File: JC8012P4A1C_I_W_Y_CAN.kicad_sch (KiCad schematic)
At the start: 0 parts

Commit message: Add CAN transceiver and 12V->5V supply schematic
CAN interface (ISOBUS, 250 kbit/s):
- TLE9250VSJ transceiver, VCC 5 V, VIO 3.3 V from FPC3 VDDA
- TXD/RXD on FPC3 pin 8/7 (GPIO4/GPIO5, as used by espVT)
- NEN on FPC3 pin 9 (GPIO3) with 10k pull-down -> normal mode by default
- Split termination 750R + 750R, 47 nF to GND (ECU Type I WEAK)
- WE-TVS 824094024 on CAN_H/CAN_L
- 10-pin box header 61201022921 -> ribbon -> IDC D-Sub 9 female
  618009221923, pinout of Mueller-Elektronik BASIC-Terminal CAN-ISO
  (fits adapter cable 481595 to In-Cab CPC-9)

Power (12 V board net only):
- Fuse 1 A slow, bidirectional TVS WE-TVSP 824551241 (SMDJ24CA)
- Reverse polarity protection: dual P-MOSFET DMP6050SSD in parallel,
  15 V gate zener, 100k gate pull-down
- Wuerth MagI3C 171030601 buck, 5.0 V / 3 A, values from datasheet p.38
- 5 V fed to the transceiver and to the base board CN2 via WR-WTB
  653104131822

Pin 8 of the TLE9250VSJ symbol renamed STB -> NEN.

Co-Authored-By: Claude Opus 5.5 <noreply@anthropic.com>
Claude-Session: https://claude.ai/code/session_014h8cGi8SRWthYdGFH1Qgzz
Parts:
- added C1: 47n, Capacitor_SMD:C_0603_1608Metric, symbol Device:C
- added C2, C3: 100n, Capacitor_SMD:C_0603_1608Metric, symbol Device:C
- added C4: 10u/50V, Capacitor_SMD:C_1210_3225Metric, symbol Device:C
- added C5: 100u/10V, Capacitor_SMD:C_1210_3225Metric, symbol Device:C
- added C6, C7: 22n, Capacitor_SMD:C_0603_1608Metric, symbol Device:C
- added D1: 824094024, JC8012P4A1C_CAN:D_Wurth_WE-TVS-SOT23-3L, symbol JC8012P4A1C_CAN:824094024
- added D2: 824551241, JC8012P4A1C_CAN:D_Wurth_WE-TVSP-DO214-AB-3000W_BI, symbol Device:D_TVS
- added D3: 15V, Diode_SMD:D_SOD-123, symbol Device:D_Zener
- added F1: 1A slow, Fuse:Fuse_1206_3216Metric, symbol Device:Fuse
- added J1: 61201022921, JC8012P4A1C_CAN:J_Wurth_WR-BHD_61201022921, symbol JC8012P4A1C_CAN:61201022921
- added J2: 68711414522, JC8012P4A1C_CAN:J_Wurth_WR-FPC_68711414522, symbol JC8012P4A1C_CAN:68711414522
- added J3: 653104131822, JC8012P4A1C_CAN:J_Wurth_WR-WTB_653104131822, symbol JC8012P4A1C_CAN:653104131822
- added Q1: DMP6050SSD, Package_SO:SOIC-8_3.9x4.9mm_P1.27mm, symbol Transistor_FET:DMP6050SSD
- added R1, R2: 750, Resistor_SMD:R_0603_1608Metric, symbol Device:R
- added R3: 10k, Resistor_SMD:R_0603_1608Metric, symbol Device:R
- added R4, R5: 100k, Resistor_SMD:R_0603_1608Metric, symbol Device:R
- added R6: 5k62, Resistor_SMD:R_0603_1608Metric, symbol Device:R
- added R7: 1k07, Resistor_SMD:R_0603_1608Metric, symbol Device:R
- added U1: TLE9250VSJ, Package_SO:SOIC-8_3.9x4.9mm_P1.27mm, symbol JC8012P4A1C_CAN:TLE9250VSJ
- added U2: 171030601, JC8012P4A1C_CAN:U_Wurth_WPME-VDRM-TO263-7EP, symbol JC8012P4A1C_CAN:171030601
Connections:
- new net +3V3: C3.1, J2.13, J2.14, U1.5 (VIO)
- new net +5V: C2.1, C5.1, C7.1, J3.1, R6.1, U1.3 (VCC), U2.7 (VOUT)
- new net BUCK_FB: C7.2, R6.2, R7.1, U2.6 (FB)
- new net BUCK_RON: R5.2, U2.2 (RON)
- new net BUCK_SS: C6.1, U2.5 (SS)
- new net CAN_H: D1.1 (I/O1), J1.4, J1.7, R1.1, U1.7 (CANH)
- new net CAN_L: D1.2 (I/O2), J1.1, J1.3, R2.2, U1.6 (CANL)
- new net CAN_NEN: J2.9, R3.1, U1.8 (NEN)
- new net CAN_RXD: J2.7, U1.4 (RXD)
- new net CAN_SPLIT: C1.1, R1.2, R2.1
- new net CAN_TXD: J2.8, U1.1 (TXD)
- new net ECU_PWR: D2.1 (A1), F1.2, Q1.5 (D2), Q1.6 (D2), Q1.7 (D1), Q1.8 (D1)
- new net ECU_PWR_IN: F1.1, J1.8
- new net GND: C1.2, C2.2, C3.2, C4.2, C5.2, C6.2, D1.3 (GND), D2.2 (A2), J1.2, J2.1, J2.2, J2.Z1, J2.Z2, J3.4, R3.2, R4.2, R7.2, U1.2 (GND), U2.4 (AGND), U2.EP (PGND)
- new net PFET_G: D3.2 (A), Q1.2 (G1), Q1.4 (G2), R4.1
- new net VIN_PROT: C4.1, D3.1 (K), Q1.1 (S1), Q1.3 (S2), R5.1, U2.1 (VIN)
- no-connect marks 0 -> 14

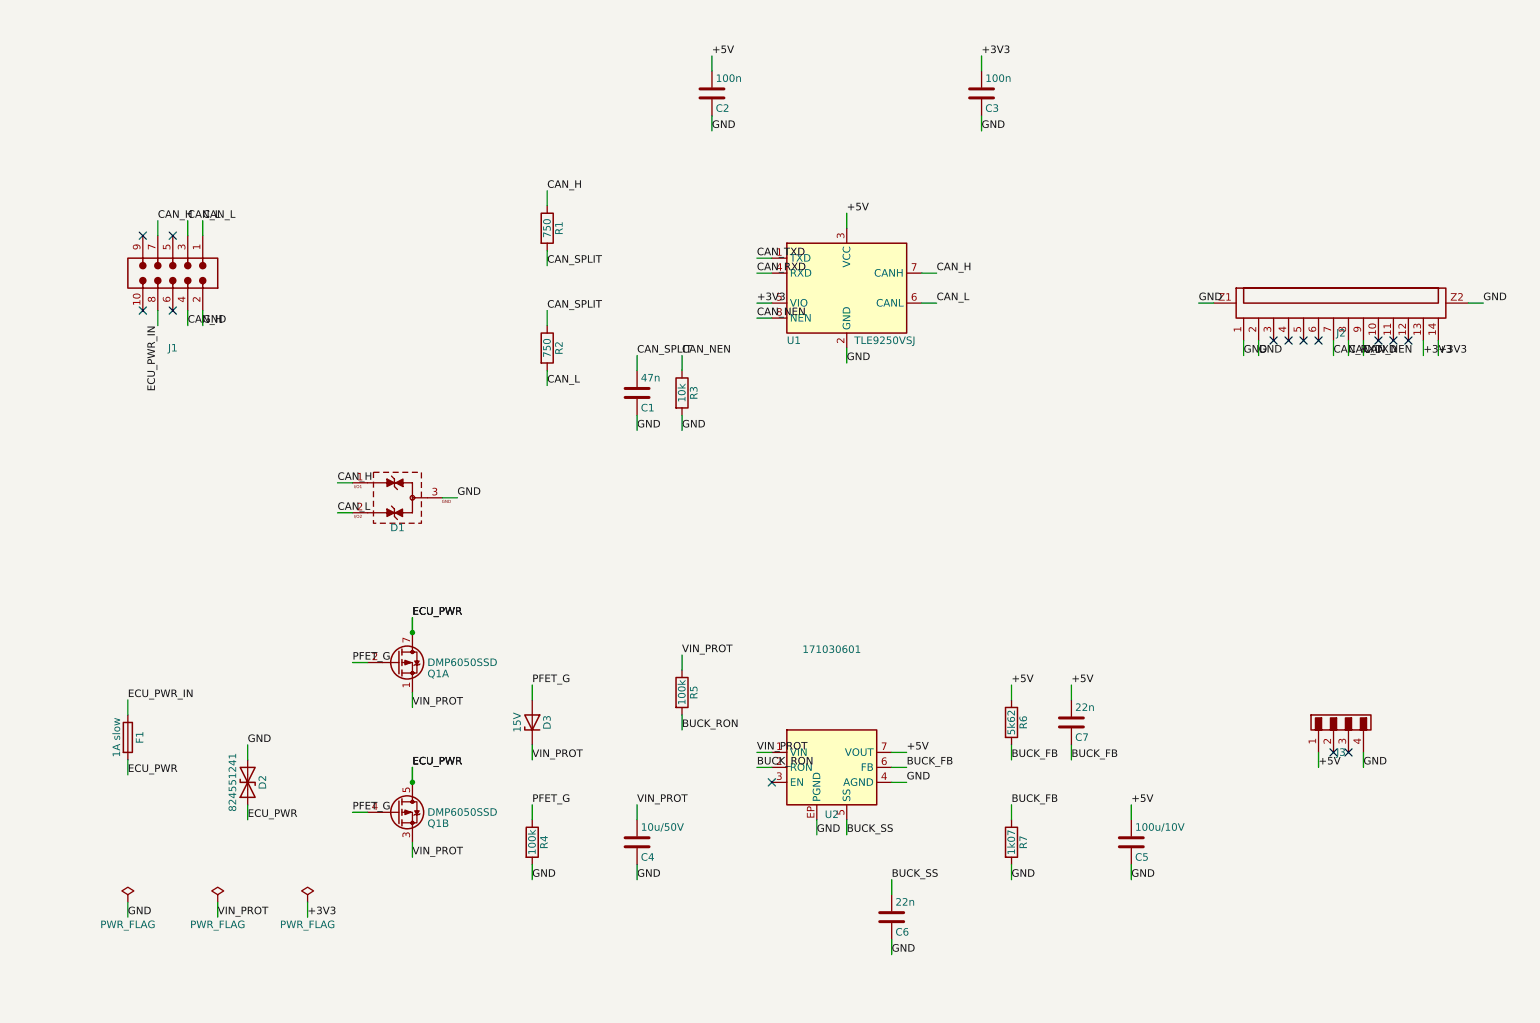
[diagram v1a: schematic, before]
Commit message: Add TBC power output, mounting holes and board outline
Schematic:
- TBC_PWR_out on D-Sub pin 8 like the Mueller-Elektronik BASIC-Terminal
  (some harnesses do not start without powered terminators):
  VIN_PROT -> SS16 Schottky (no back-feed) -> PTC 0.14 A -> J1 pin 6
- TBC_GND (D-Sub pin 3) to GND via R8 0R, DNP by default to stay
  compatible; fit R8 only if a harness needs the TBC_GND return
- Mounting holes H1-H4, M2, 2.2 mm (ISO 273 medium)
- Labels oriented away from pins, overlapping parts moved apart
  (netlist unchanged)

Board:
- Footprints imported from schematic (not placed yet)
- Outline 66 x 54 mm (provisional), holes on 58 x 46 mm grid,
  4 mm from the edge

Co-Authored-By: Claude Opus 5.5 <noreply@anthropic.com>
Claude-Session: https://claude.ai/code/session_014h8cGi8SRWthYdGFH1Qgzz
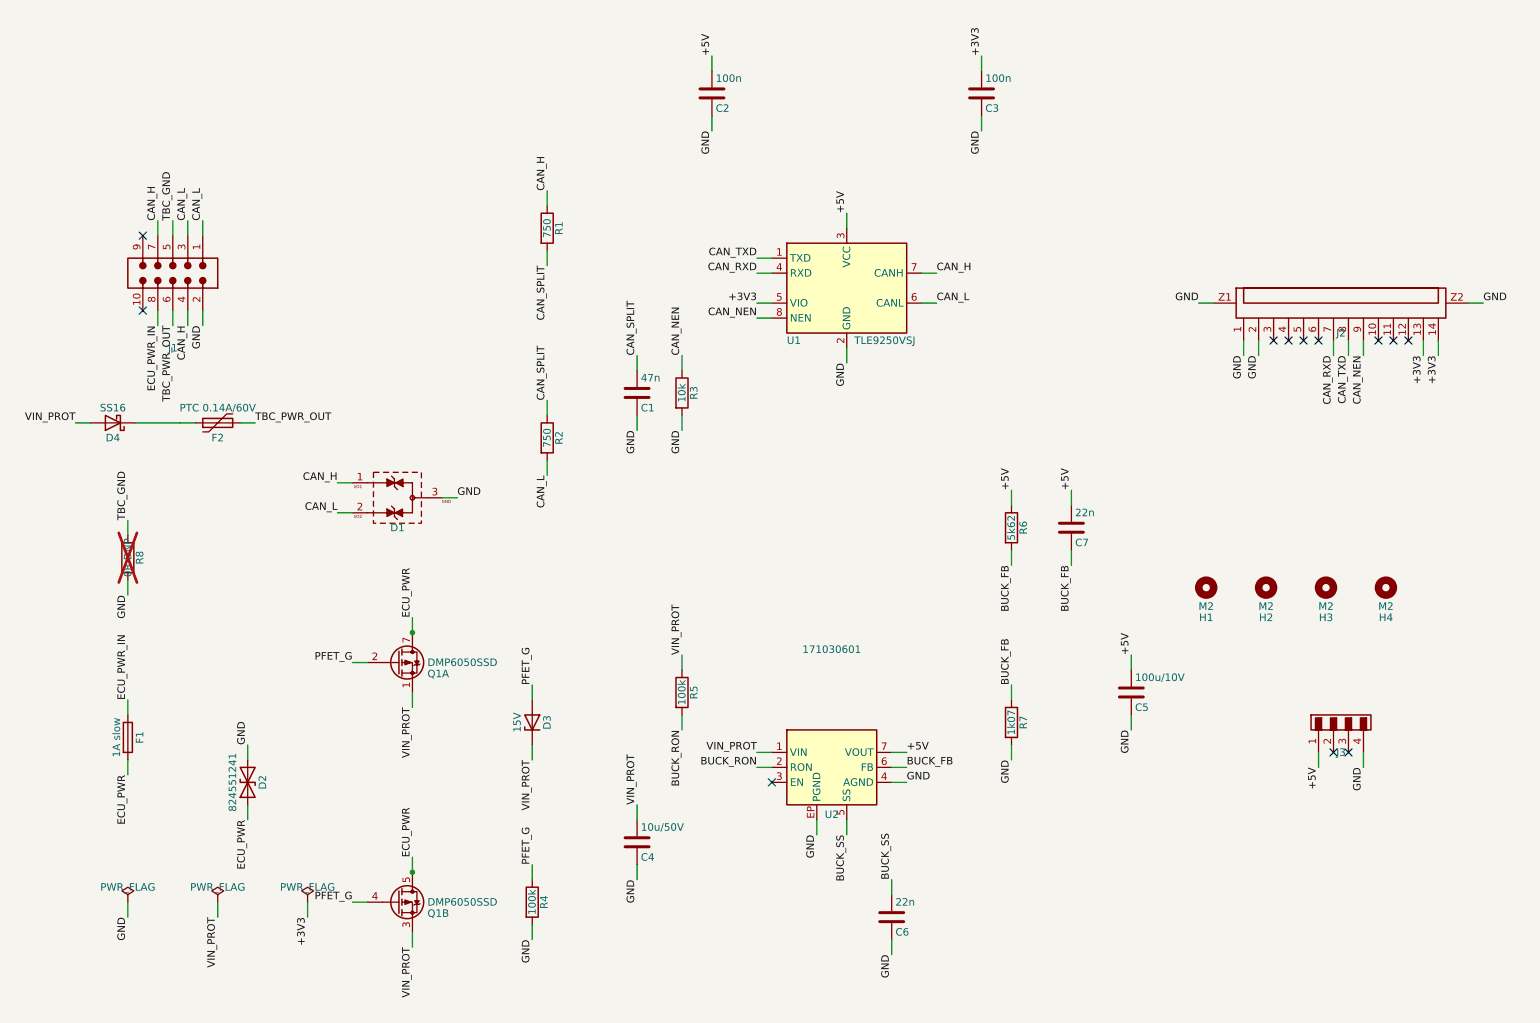
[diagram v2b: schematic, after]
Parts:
- added D4: SS16, Diode_SMD:D_SMA, symbol Device:D_Schottky
- added F2: PTC 0.14A/60V, Fuse:Fuse_1812_4532Metric, symbol Device:Polyfuse
- added H1, H2, H3, H4: M2, MountingHole:MountingHole_2.2mm_M2, symbol Mechanical:MountingHole
- added R8: 0R DNP, Resistor_SMD:R_0603_1608Metric, symbol Device:R
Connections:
- net GND: now also R8.2
- net VIN_PROT: now also D4.2 (A)
- net TBC_GND: now reaches J1.5
- net TBC_GND: now also R8.1
- net TBC_PWR_OUT: now reaches J1.6
- net TBC_PWR_OUT: now also F2.2
- new net: D4.1 (K), F2.1
- no-connect marks 14 -> 12
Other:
- moved on the sheet: C5, C7, Q1B, R2, R4, R6, R7

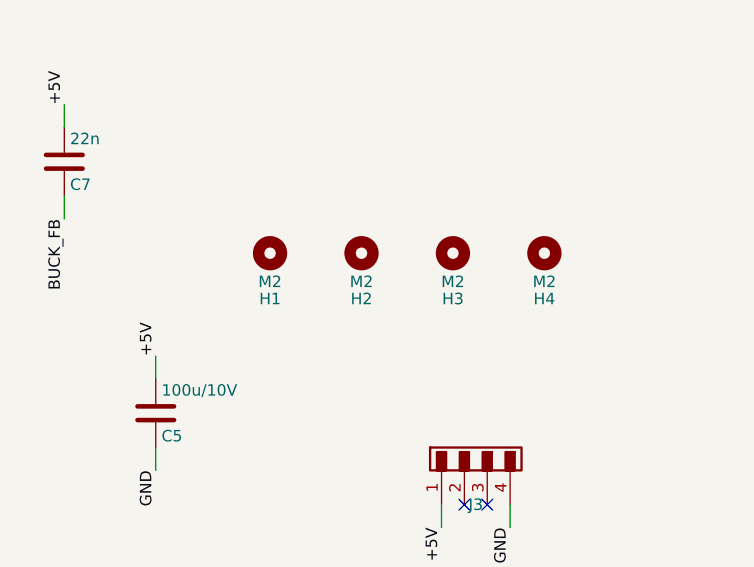
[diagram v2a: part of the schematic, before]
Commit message: Plate mounting holes to GND, fix PCB footprint links, add README
- H1-H4: MountingHole_Pad symbol, footprint MountingHole_2.2mm_M2_Pad_Via
  connected to GND (ground via the brass standoffs to the display
  board); excluded from BOM and position files
- PCB re-imported with KiCad "Update PCB from Schematic" (F8):
  footprints now linked to their symbols, net names /GND etc.,
  R8 marked DNP. The earlier import via KiCAD-MCP-Server created
  unlinked footprints.
- README: connectors, D-Sub 9 / J1 pinout, FPC3 pinout, termination,
  TBC power output and R8 (DNP by default, fit 0R if a harness needs
  the TBC_GND return), power section

Co-Authored-By: Claude Opus 5.5 <noreply@anthropic.com>
Claude-Session: https://claude.ai/code/session_014h8cGi8SRWthYdGFH1Qgzz
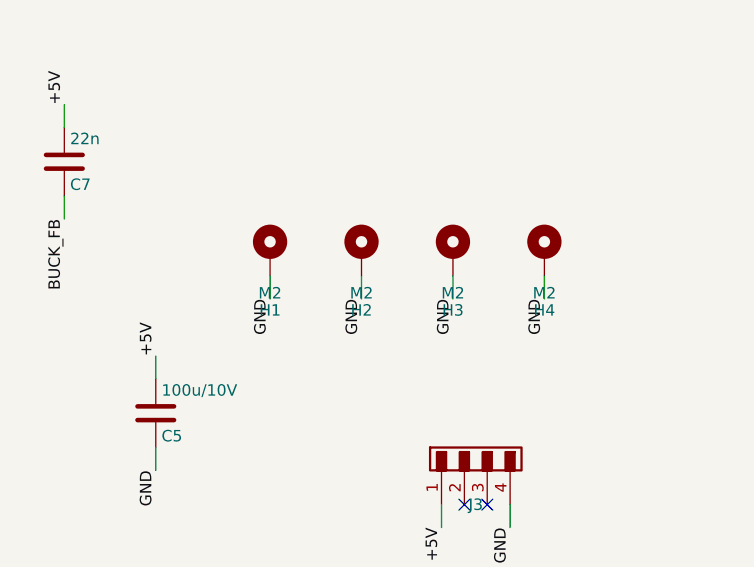
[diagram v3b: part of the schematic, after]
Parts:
- removed H1, H2, H3, H4: M2, MountingHole:MountingHole_2.2mm_M2, symbol Mechanical:MountingHole
- added H1, H2, H3, H4: M2, MountingHole:MountingHole_2.2mm_M2_Pad_Via, symbol Mechanical:MountingHole_Pad
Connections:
- net GND: now also H1.1, H2.1, H3.1, H4.1

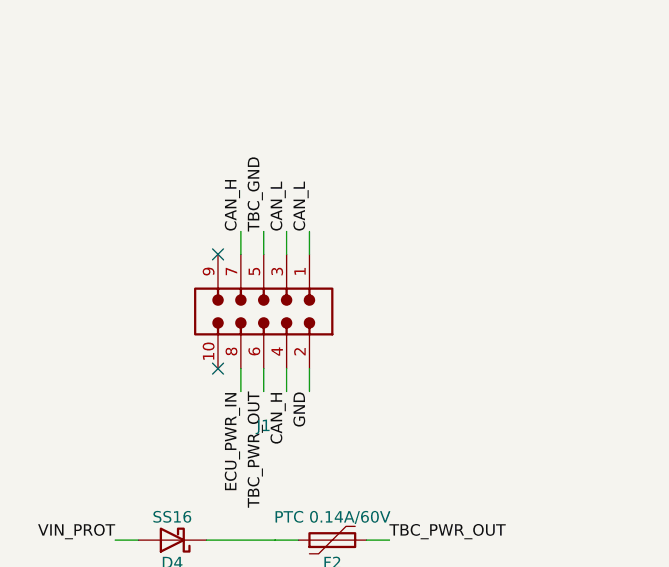
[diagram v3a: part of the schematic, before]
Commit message: J1: SMT right-angled pin header instead of THT box header
- J1 is now Wuerth WR-PHD 610110249121 (2x5, 2.54 mm, SMT, right
  angled, 6.5 mm high). The former WR-BHD 61201022921 was a THT angled
  box header with long levers (32 x 28 mm) and too big; a straight SMT
  box header would be too high (only ~8 mm free under the cover).
  The board is now SMT only, all parts on the top side.
- Same pinout, J1 rewired in the schematic (netlist checked)
- J1 placed at the bottom edge left of the CR1220 notch, pins towards
  the edge (ribbon cable leaves downwards)
- Polarisation without shroud: cut pin 10 and close position 10 of the
  IDC socket with a coding plug (pins 9/10 unused), see README
- README: mechanics section (stack height, holes, notches)
- Old part removed from the project library

Co-Authored-By: Claude Opus 5.5 <noreply@anthropic.com>
Claude-Session: https://claude.ai/code/session_014h8cGi8SRWthYdGFH1Qgzz
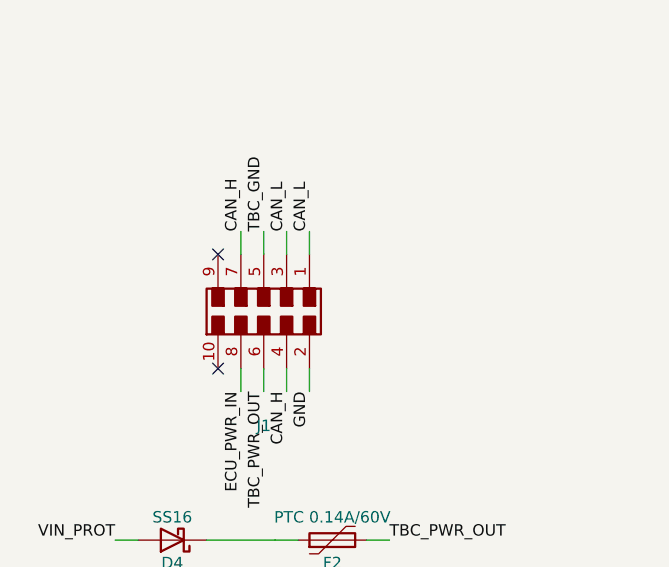
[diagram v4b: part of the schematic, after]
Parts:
- removed J1: 61201022921, JC8012P4A1C_CAN:J_Wurth_WR-BHD_61201022921, symbol JC8012P4A1C_CAN:61201022921
- added J1: 610110249121, JC8012P4A1C_CAN:J_Wurth_WR-PHD_610110249121, symbol JC8012P4A1C_CAN:610110249121
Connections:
- net CAN_H: now also J1.4, J1.7
- net CAN_L: now also J1.1, J1.3
- net ECU_PWR_IN: now also J1.8
- net GND: now also J1.2
- net TBC_GND: now also J1.5
- net TBC_PWR_OUT: now also J1.6

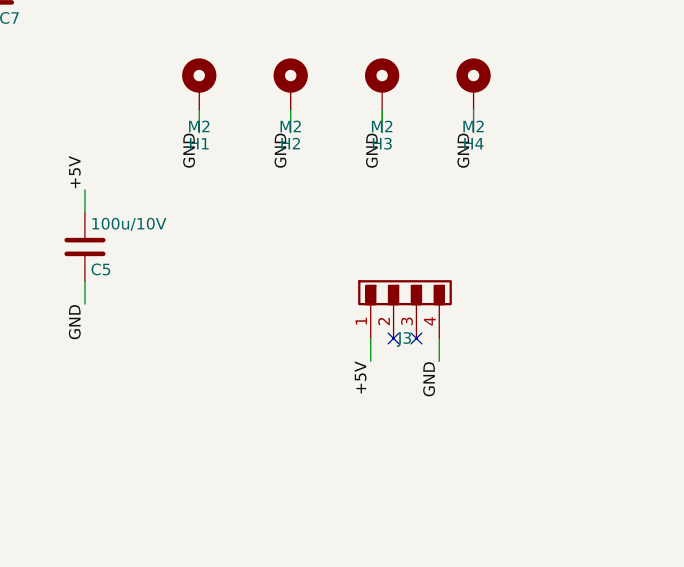
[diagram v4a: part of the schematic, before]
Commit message: J3 mounting tabs to GND, J1 flush with the board edge
- J3 (WR-WTB 653104131822) symbol: added pins MP1/MP2 for the solder
  tabs of the footprint, connected to GND. Removes the two F8 warnings
  "no net for J3 pad MP1/MP2".
- J1 moved so that the plastic body is flush with the bottom board
  edge; only the pins stick out, so the IDC socket can be plugged in.
  The two 1.8 mm locating holes are 0.37 mm from the routed edge
  (JLCPCB states no NPTH-to-edge rule; a broken web is harmless).

Co-Authored-By: Claude Opus 5.5 <noreply@anthropic.com>
Claude-Session: https://claude.ai/code/session_014h8cGi8SRWthYdGFH1Qgzz
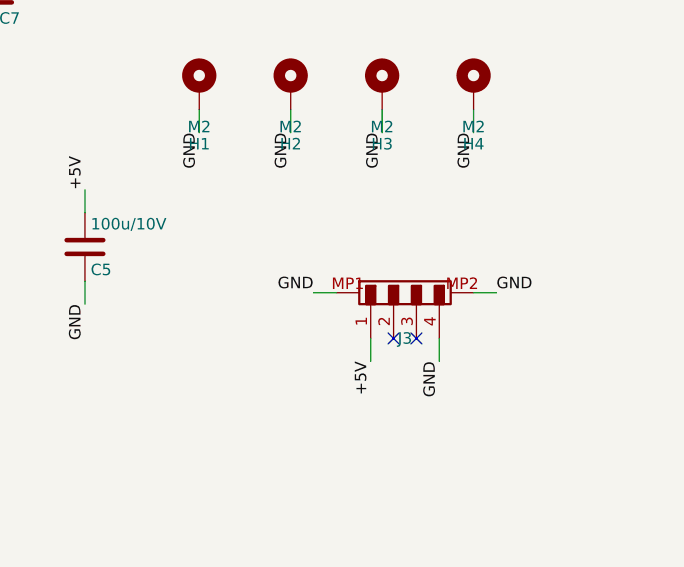
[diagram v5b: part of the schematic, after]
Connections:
- net GND: now also J3.MP1 (MP), J3.MP2 (MP)
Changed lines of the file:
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@@
 		(at 33.02 82.55)
+	)
+	(wire
+		(pts
+			(xy 228.6 152.4) (xy 226.06 152.4)
+		)
+		(stroke
+			(width 0)
+			(type default)
+		)
+	)
+	(label "GND"
+		(at 226.06 152.4 180)
+		(effects
+			(font
+				(size 1.27 1.27)
+			)
+			(justify right bottom)
+		)
+	)
+	(wire
+		(pts
+			(xy 243.84 152.4) (xy 246.38 152.4)
+		)
+		(stroke
+			(width 0)
+			(type default)
+		)
+	)
+	(label "GND"
+		(at 246.38 152.4 0)
+		(effects
+			(font
+				(size 1.27 1.27)
+			)
+			(justify left bottom)
+		)
 	)
 	(sheet_instances
